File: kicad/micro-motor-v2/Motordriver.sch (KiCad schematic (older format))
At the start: 24 parts, among them Q401 FDMD82xx, Q402 FDMD82xx, Q403 FDMD82xx, U401 DRV8320S, U402 INA240A2PW, U403 INA240A2PW, U404 INA240A2PW

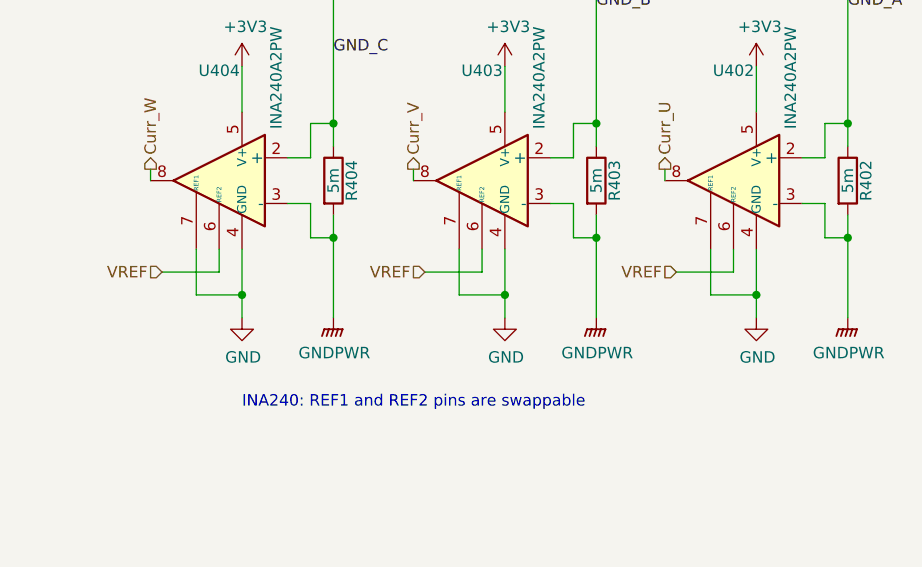
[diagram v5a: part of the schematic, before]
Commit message: micro-motor-v2: Layout finished
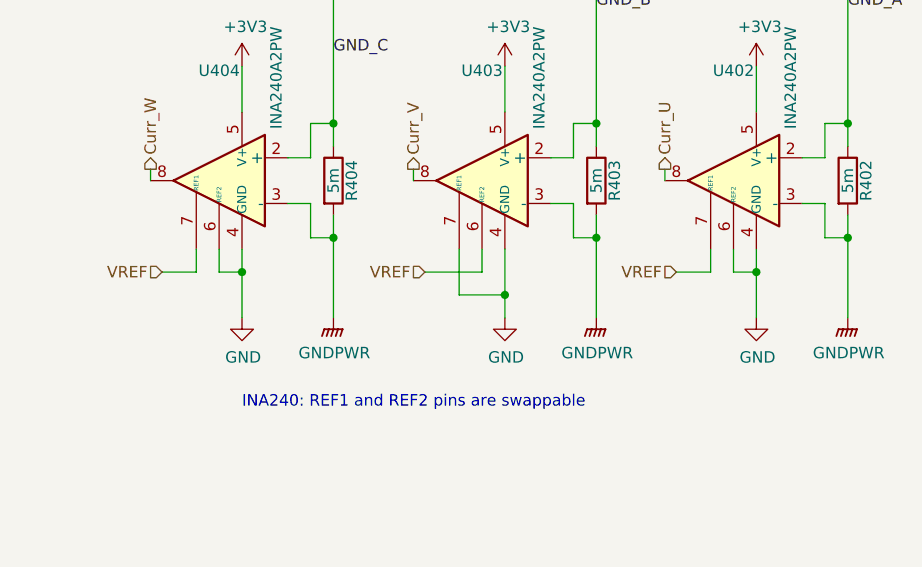
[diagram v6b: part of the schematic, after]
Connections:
- net GND: now also U402.6 (REF2), U404.6 (REF2); no longer U402.7 (REF1), U404.7 (REF1)
- net VREF: now also U402.7 (REF1), U404.7 (REF1); no longer U402.6 (REF2), U404.6 (REF2)
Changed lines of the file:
@@
 Curr_U
-Wire Wire Line
-	9000 5600 9000 5800
-Wire Wire Line
-	9000 5800 9200 5800
 Wire Wire Line
 	9400 5400 9500 5400
@@
 Wire Wire Line
 	9600 5050 9600 5150
-Wire Wire Line
-	9100 5600 9100 5700
 Wire Wire Line
 	7350 5450 7350 5550
@@
 Curr_W
 Wire Wire Line
-	6750 5600 6750 5800
-Wire Wire Line
-	6750 5800 6950 5800
-Wire Wire Line
-	6950 5800 6950 5600
-Wire Wire Line
 	7150 5400 7250 5400
 Wire Wire Line
@@
 Wire Wire Line
 	7350 5050 7350 5150
-Wire Wire Line
-	6850 5600 6850 5700
-Wire Wire Line
-	6850 5700 6600 5700
 Connection ~ 7350 4400
 Wire Wire Line
@@
 VREF
 Wire Wire Line
-	9200 5800 9200 5600
-Wire Wire Line
-	8850 5700 9100 5700
-Wire Wire Line
 	7750 5700 8000 5700
 Text Notes 6950 6300 0    50   ~ 0
@@
 $EndComp
 Wire Wire Line
-	9200 5900 9200 5800
-Connection ~ 9200 5800
-Wire Wire Line
 	8100 5800 8100 5900
 Connection ~ 8100 5800
-Wire Wire Line
-	6950 5800 6950 5900
-Connection ~ 6950 5800
 $Comp
 L power:GND #PWR0125
@@
 	1    0    0    -1
 $EndComp
+Wire Wire Line
+	6950 5600 6950 5700
+Wire Wire Line
+	6600 5700 6750 5700
+Wire Wire Line
+	6750 5700 6750 5600
+Wire Wire Line
+	6850 5600 6850 5700
+Wire Wire Line
+	6850 5700 6950 5700
+Connection ~ 6950 5700
+Wire Wire Line
+	6950 5700 6950 5900
+Wire Wire Line
+	9200 5600 9200 5700
+Wire Wire Line
+	8850 5700 9000 5700
+Wire Wire Line
+	9000 5700 9000 5600
+Wire Wire Line
+	9100 5600 9100 5700
+Wire Wire Line
+	9100 5700 9200 5700
+Connection ~ 9200 5700
+Wire Wire Line
+	9200 5700 9200 5900
 $EndSCHEMATC
